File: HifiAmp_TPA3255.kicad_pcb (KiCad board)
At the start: 4 copper layers, 200 x 150 mm, 124 parts, among them J1 PVDD 48V IN — NEEDS_DATA, J2 RCA L SE, J3 RCA R SE, J301 SPK_L, J302 SPK_R, J4 VOLUME_REMOTE, Q301 IPP330P10NM, Q302 IXTK200N10L2, U1 LM5010ASD, U2 LM2940IMP-12/NOPB, U3 TLV1117-33IDCY, U4 OPA1612AIDR, U5 OPA1612AIDR, U6 TPA3255B, U7 TPS3802K33DCKR, U8 LM5069-2

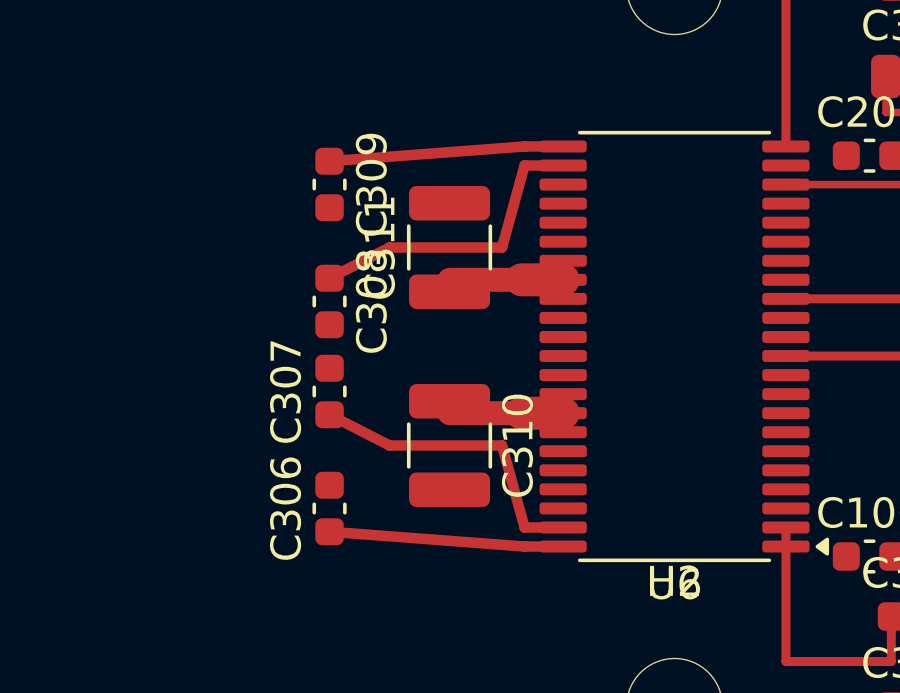
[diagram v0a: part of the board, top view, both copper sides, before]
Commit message: feat(f1.2-b1): flip C310 and C311 to the back, by tool rather than by hand
The gesture that blocked this task was never available: no MCP tool returned a
placed footprint to the other side, and edit_component accepted a layer field
it silently ignored. Konnect v1.2.0 ships flip_component, so the flip is a tool
call again — file-mode, refused while KiCAD holds the board, geometry mirrored
the way KiCAD mirrors it.

Proof is KiCAD's, not ours: kicad-cli pcb export pos reports C310 and C311 as
bottom. The board md5 moves 2cc389a5..1bef -> 619eedd7..a1c1, 124 footprints
preserved.

The PVDD reroute through vias under U6 is the other half of f1.2-b1 and needs
the running editor; it is not in this commit.
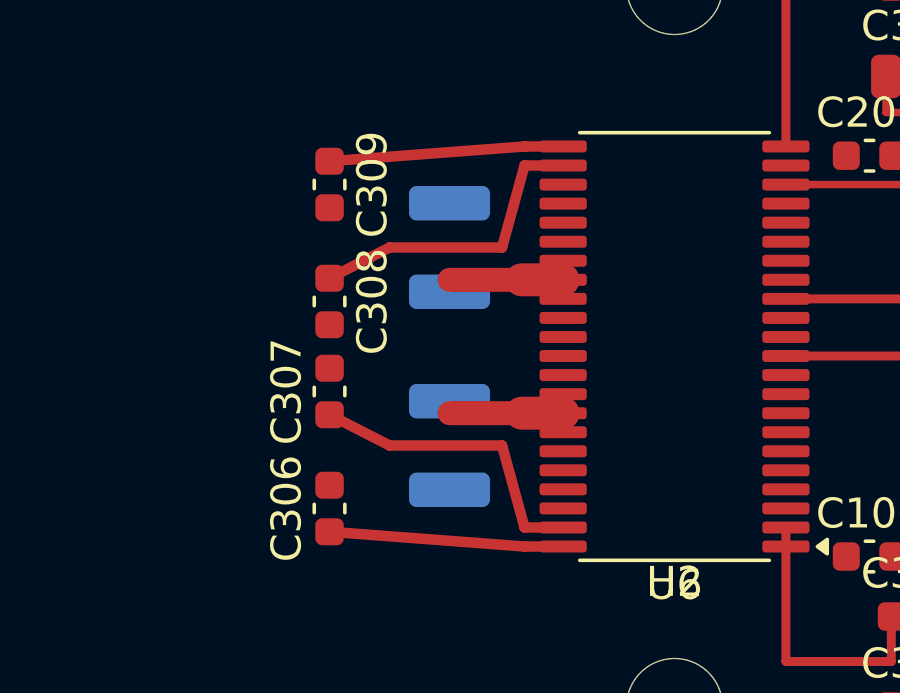
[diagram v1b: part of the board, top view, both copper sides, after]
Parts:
- C310, C311: moved to B.Cu
- turned C310 to 90 degrees
- turned C311 to -90 degrees
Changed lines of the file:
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@@
 	)
 	(footprint "Capacitor_SMD:C_1210_3225Metric"
-		(layer "F.Cu")
-		(at 277.5 178.3 -90)
+		(layer "B.Cu")
+		(at 277.5 178.3 90)
 		(descr "Capacitor SMD 1210 (3225 Metric), square (rectangular) end terminal, IPC-7351 nominal, (Body size source: IPC-SM-782 page 76, https://www.pcb-3d.com/wordpress/wp-content/uploads/ipc-sm-782a_amendment_1_and_2.pdf)")
 		(tags "capacitor")
 		(property "Reference" "C310"
-			(at 0 -2.3 270)
-			(layer "F.SilkS")
+			(at 0 2.3 270)
+			(layer "B.SilkS")
 			(effects
 				(font
@@
 					(thickness 0.15)
 				)
-			)
+			 (justify mirror))
 		)
 		(property "Value" "1uF/100V"
-			(at 0 2.3 270)
-			(layer "F.Fab")
+			(at 0 -2.3 270)
+			(layer "B.Fab")
 			(effects
 				(font
@@
 					(thickness 0.15)
 				)
-			)
+			 (justify mirror))
 		)
 		(property "Datasheet" ""
 			(at 0 0 270)
-			(layer "F.Fab")
+			(layer "B.Fab")
 			(hide yes)
 			(effects
@@
 					(size 1.27 1.27)
 				)
-			)
+			 (justify mirror))
 		)
 		(property "Description" ""
 			(at 0 0 270)
-			(layer "F.Fab")
+			(layer "B.Fab")
 			(hide yes)
 			(effects
@@
 					(size 1.27 1.27)
 				)
-			)
+			 (justify mirror))
 		)
 		(property "KiLib_Generator" "SMD_2terminal_chip_molded"
 			(at 0 0 270)
-			(layer "F.SilkS")
+			(layer "B.SilkS")
 			(hide yes)
 			(effects
@@
 					(thickness 0.15)
 				)
-			)
+			 (justify mirror))
 		)
 		(property ki_fp_filters "C_*")
@@
 		(duplicate_pad_numbers_are_jumpers no)
 		(fp_line
-			(start -0.711252 1.36)
-			(end 0.711252 1.36)
+			(start -0.711252 -1.36)
+			(end 0.711252 -1.36)
 			(stroke
 				(width 0.12)
 				(type solid)
 			)
-			(layer "F.SilkS")
+			(layer "B.SilkS")
 		)
 		(fp_line
-			(start -0.711252 -1.36)
-			(end 0.711252 -1.36)
+			(start -0.711252 1.36)
+			(end 0.711252 1.36)
 			(stroke
 				(width 0.12)
 				(type solid)
 			)
-			(layer "F.SilkS")
+			(layer "B.SilkS")
 		)
 		(fp_rect
-			(start -2.3 -1.6)
-			(end 2.3 1.6)
+			(start -2.3 1.6)
+			(end 2.3 -1.6)
 			(stroke
 				(width 0.05)
@@
 			)
 			(fill no)
-			(layer "F.CrtYd")
+			(layer "B.CrtYd")
 		)
 		(fp_rect
-			(start -1.6 -1.25)
-			(end 1.6 1.25)
+			(start -1.6 1.25)
+			(end 1.6 -1.25)
 			(stroke
 				(width 0.1)
@@
 			)
 			(fill no)
-			(layer "F.Fab")
+			(layer "B.Fab")
 		)
 		(fp_text user "${REFERENCE}"
 			(at 0 0 270)
-			(layer "F.Fab")
+			(layer "B.Fab")
 			(effects
 				(font
@@
 					(thickness 0.12)
 				)
-			)
+			 (justify mirror))
 		)
 		(pad "1" smd roundrect
-			(at -1.475 0 270)
+			(at -1.475 0 90)
 			(size 1.15 2.7)
-			(layers "F.Cu" "F.Mask" "F.Paste")
+			(layers "B.Cu" "B.Mask" "B.Paste")
 			(roundrect_rratio 0.217391)
 			(net "/PVDD")
@@
 		)
 		(pad "2" smd roundrect
-			(at 1.475 0 270)
+			(at 1.475 0 90)
 			(size 1.15 2.7)
-			(layers "F.Cu" "F.Mask" "F.Paste")
+			(layers "B.Cu" "B.Mask" "B.Paste")
 			(roundrect_rratio 0.217391)
 			(net "/GND")
@@
 	)
 	(footprint "Capacitor_SMD:C_1210_3225Metric"
-		(layer "F.Cu")
-		(at 277.5 171.7 90)
+		(layer "B.Cu")
+		(at 277.5 171.7 -90)
 		(descr "Capacitor SMD 1210 (3225 Metric), square (rectangular) end terminal, IPC-7351 nominal, (Body size source: IPC-SM-782 page 76, https://www.pcb-3d.com/wordpress/wp-content/uploads/ipc-sm-782a_amendment_1_and_2.pdf)")
 		(tags "capacitor")
 		(property "Reference" "C311"
-			(at 0 -2.3 90)
-			(layer "F.SilkS")
+			(at 0 2.3 90)
+			(layer "B.SilkS")
 			(effects
 				(font
@@
 					(thickness 0.15)
 				)
-			)
+			 (justify mirror))
 		)
 		(property "Value" "1uF/100V"
-			(at 0 2.3 90)
-			(layer "F.Fab")
+			(at 0 -2.3 90)
+			(layer "B.Fab")
 			(effects
 				(font
@@
 					(thickness 0.15)
 				)
-			)
+			 (justify mirror))
 		)
 		(property "Datasheet" ""
 			(at 0 0 90)
-			(layer "F.Fab")
+			(layer "B.Fab")
 			(hide yes)
 			(effects
@@
 					(size 1.27 1.27)
 				)
-			)
+			 (justify mirror))
 		)
 		(property "Description" ""
 			(at 0 0 90)
-			(layer "F.Fab")
+			(layer "B.Fab")
 			(hide yes)
 			(effects
@@
 					(size 1.27 1.27)
 				)
-			)
+			 (justify mirror))
 		)
 		(property "KiLib_Generator" "SMD_2terminal_chip_molded"
 			(at 0 0 90)
-			(layer "F.SilkS")
+			(layer "B.SilkS")
 			(hide yes)
 			(effects
@@
 					(thickness 0.15)
 				)
-			)
+			 (justify mirror))
 		)
 		(property ki_fp_filters "C_*")
@@
 		(duplicate_pad_numbers_are_jumpers no)
 		(fp_line
-			(start -0.711252 -1.36)
-			(end 0.711252 -1.36)
+			(start -0.711252 1.36)
+			(end 0.711252 1.36)
 			(stroke
 				(width 0.12)
 				(type solid)
 			)
-			(layer "F.SilkS")
+			(layer "B.SilkS")
 		)
 		(fp_line
-			(start -0.711252 1.36)
-			(end 0.711252 1.36)
+			(start -0.711252 -1.36)
+			(end 0.711252 -1.36)
 			(stroke
 				(width 0.12)
 				(type solid)
 			)
-			(layer "F.SilkS")
+			(layer "B.SilkS")
 		)
 		(fp_rect
-			(start -2.3 -1.6)
-			(end 2.3 1.6)
+			(start -2.3 1.6)
+			(end 2.3 -1.6)
 			(stroke
 				(width 0.05)
@@
 			)
 			(fill no)
-			(layer "F.CrtYd")
+			(layer "B.CrtYd")
 		)
 		(fp_rect
-			(start -1.6 -1.25)
-			(end 1.6 1.25)
+			(start -1.6 1.25)
+			(end 1.6 -1.25)
 			(stroke
 				(width 0.1)
@@
 			)
 			(fill no)
-			(layer "F.Fab")
+			(layer "B.Fab")
 		)
 		(fp_text user "${REFERENCE}"
 			(at 0 0 90)
-			(layer "F.Fab")
+			(layer "B.Fab")
 			(effects
 				(font
@@
 					(thickness 0.12)
 				)
-			)
+			 (justify mirror))
 		)
 		(pad "1" smd roundrect
-			(at -1.475 0 90)
+			(at -1.475 0 270)
 			(size 1.15 2.7)
-			(layers "F.Cu" "F.Mask" "F.Paste")
+			(layers "B.Cu" "B.Mask" "B.Paste")
 			(roundrect_rratio 0.217391)
 			(net "/PVDD")
@@
 		)
 		(pad "2" smd roundrect
-			(at 1.475 0 90)
+			(at 1.475 0 270)
 			(size 1.15 2.7)
-			(layers "F.Cu" "F.Mask" "F.Paste")
+			(layers "B.Cu" "B.Mask" "B.Paste")
 			(roundrect_rratio 0.217391)
 			(net "/GND")
